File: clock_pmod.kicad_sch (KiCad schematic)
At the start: 7 parts, among them IC1 ECP5-BGA256, Y1 Osc60MHz

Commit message: rename libraries from luna to cynthion
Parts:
- IC1: footprint luna:lattice_cabga256 -> cynthion:lattice_cabga256
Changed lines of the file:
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@@
       (effects (font (size 1.27 1.27)) (justify right))
     )
-    (property "Footprint" "luna:lattice_cabga256" (id 2) (at -25.4 -38.1 0)
+    (property "Footprint" "cynthion:lattice_cabga256" (id 2) (at -25.4 -38.1 0)
       (effects (font (size 1.27 1.27)) (justify left) hide)
     )

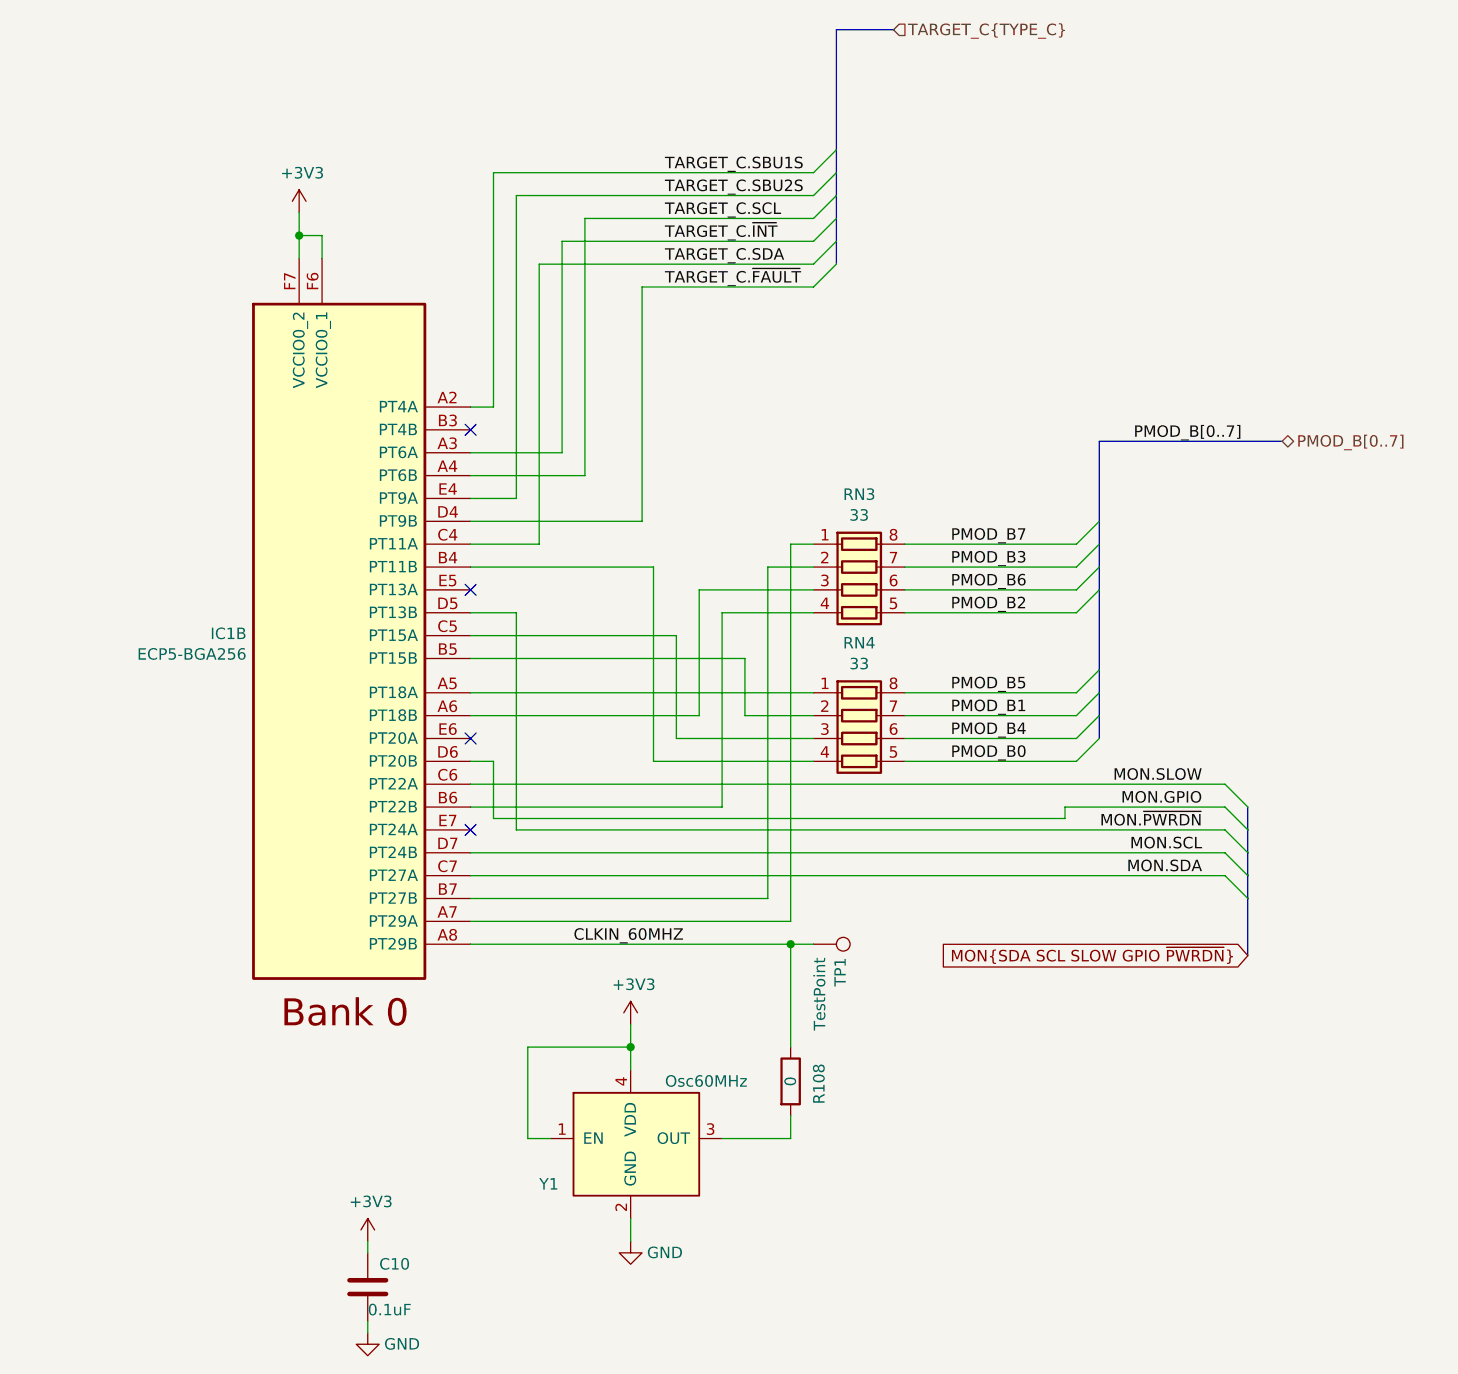
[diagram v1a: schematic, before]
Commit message: Add pseudo-VCCIO and pseudo-GND pins, decoupling
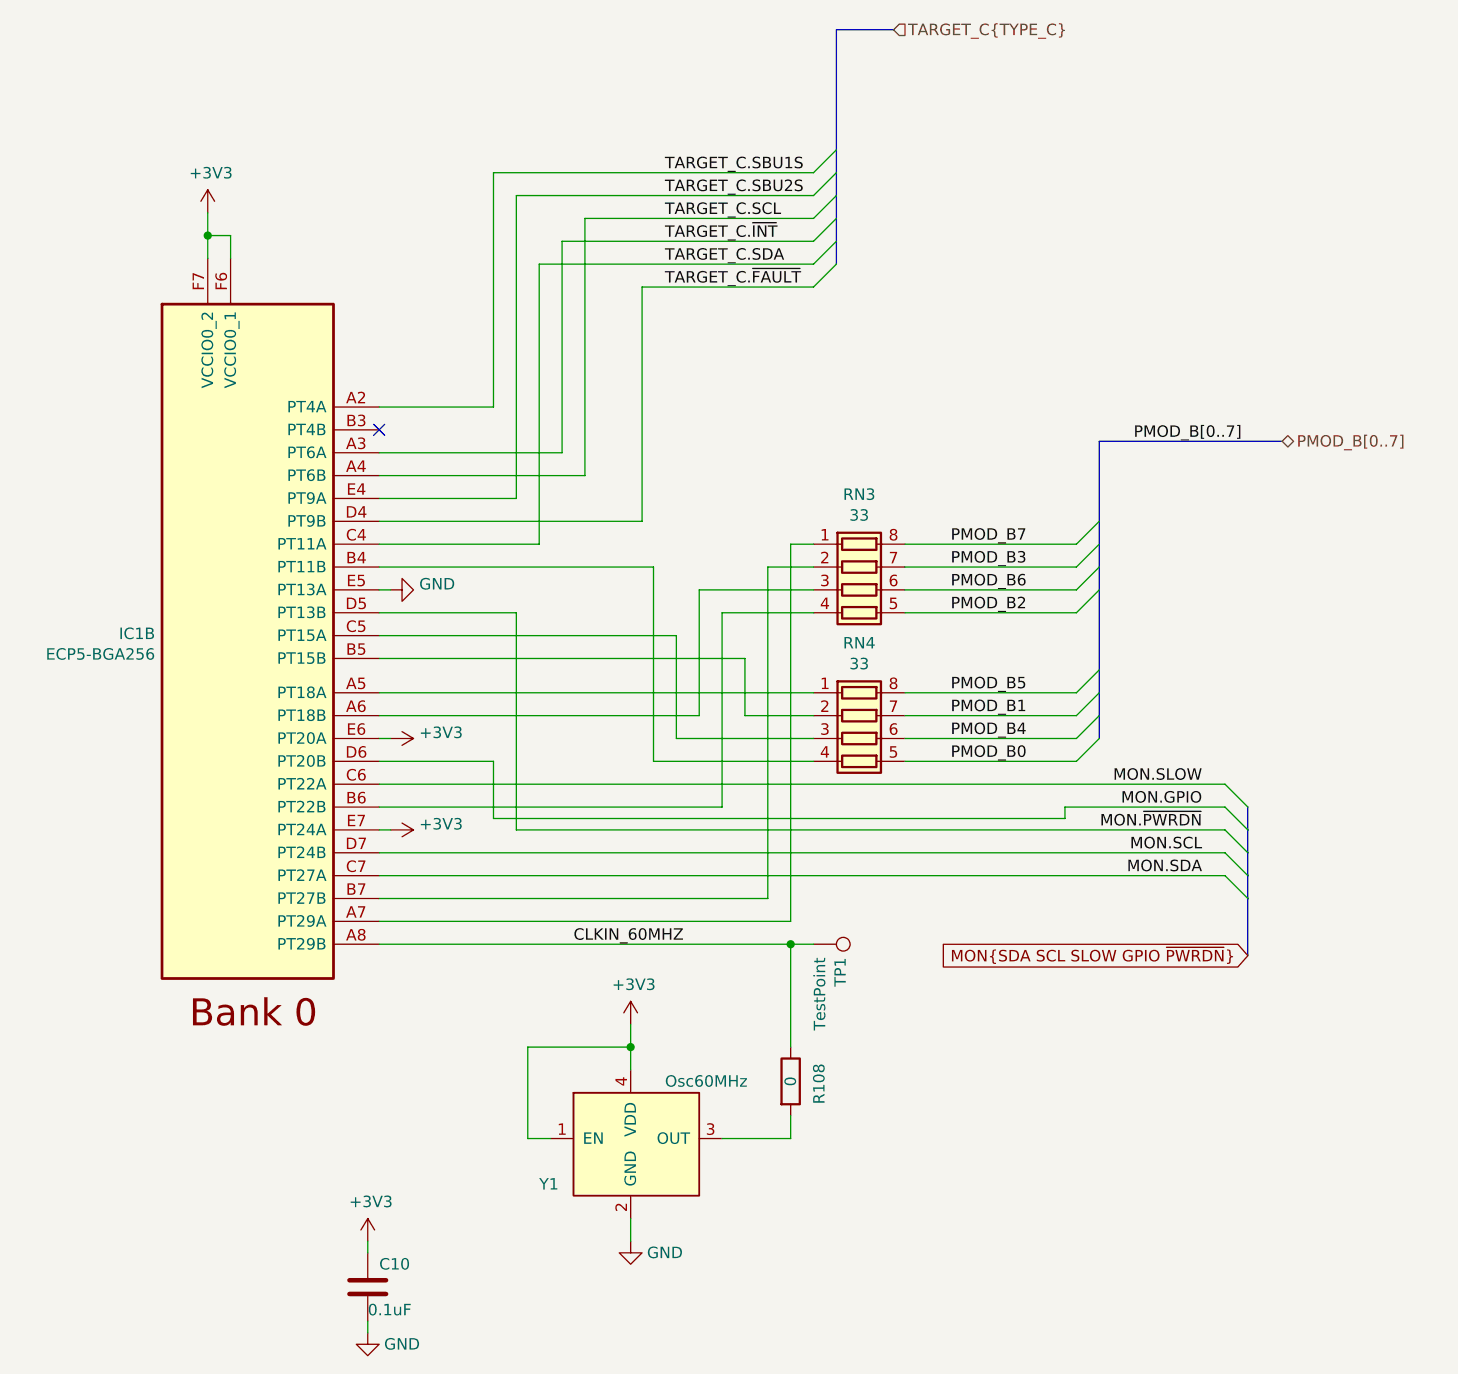
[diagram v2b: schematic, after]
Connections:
- net +3V3: now also IC1.E6 (PT20A), IC1.E7 (PT24A)
- net GND: now also IC1.E5 (PT13A)
- no-connect marks 4 -> 1
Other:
- moved on the sheet: IC1B

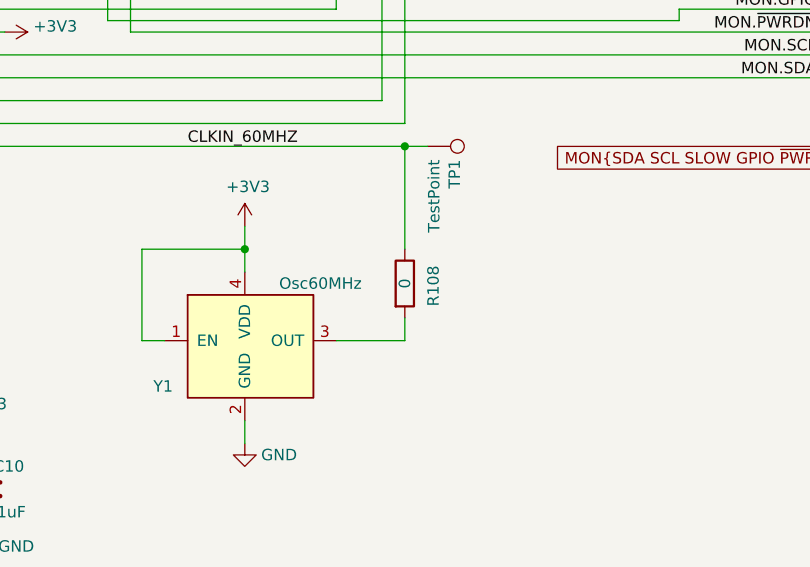
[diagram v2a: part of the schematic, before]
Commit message: Add oscillator series resistance (R108)
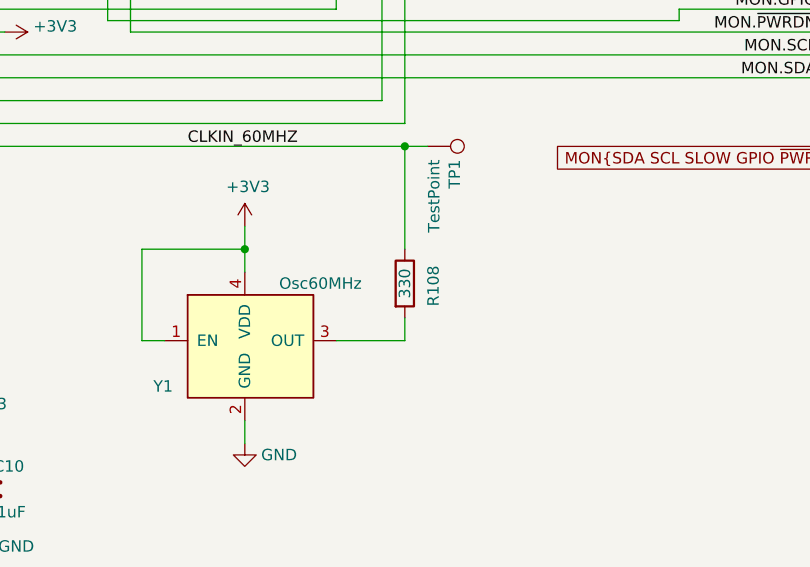
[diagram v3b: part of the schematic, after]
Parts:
- R108: value 0 -> 330; Part Number RC0402FR-070RL -> RC0402FR-13330RL
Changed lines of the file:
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@@
       (effects (font (size 1.27 1.27)) (justify left))
     )
-    (property "Value" "0" (id 1) (at 115.57 135.89 90))
+    (property "Value" "330" (id 1) (at 115.57 135.89 90))
     (property "Footprint" "Resistor_SMD:R_0402_1005Metric" (id 2) (at 113.792 135.89 90)
       (effects (font (size 1.27 1.27)) hide)
@@
       (effects (font (size 1.27 1.27)) hide)
     )
-    (property "Part Number" "RC0402FR-070RL" (id 4) (at 115.57 135.89 0)
+    (property "Part Number" "RC0402FR-13330RL" (id 4) (at 115.57 135.89 0)
       (effects (font (size 1.27 1.27)) hide)
     )
@@
       (effects (font (size 1.27 1.27)) hide)
     )
-    (property "Description" "RES 0 OHM JUMPER 1/16W 0402" (id 6) (at 115.57 135.89 0)
+    (property "Description" "RES 330 OHM 1% 1/16W 0402" (id 6) (at 115.57 135.89 0)
       (effects (font (size 1.27 1.27)) hide)
     )
